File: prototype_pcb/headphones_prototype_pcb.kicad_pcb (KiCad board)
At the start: 2 copper layers, 59.8 x 62.2 mm, 52 parts, among them J1 LIGHTING_JACK, J2 CONN_01X10, J3 BOTTOM_FLEX_LIGHTNING, J4 CONN_01X10, J5 LIGHTNING_HEADPHONE_ADAPTER, J6 CONN_01X10, J7 IPHONE_HEADPHONE_JACK, J8 CONN_01X02, U1 SN74LVC1G123, U2 ADG774A, U3 SN74LVC1G123, U4 NC7S32

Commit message: Rigid prototype pcb v1.2
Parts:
- added J10: CONN_01X05, Pin_Headers:Pin_Header_Straight_1x05_Pitch2.54mm, F.Cu at (120.3, 128.8)
- added J9: LIGHTNING_HEADPHONE_ADAPTER, lightning_headphone_adapter:LIGHTNING_HEADPHONE_ADAPTER_HANDWIRE, F.Cu at (109.1, 83.3)
- J5: footprint lightning_headphone_adapter:LIGHTNING_HEADPHONE_ADAPTER -> lightning_headphone_adapter:LIGHTNING_HEADPHONE_ADAPTER_CASTELLATED
- moved J7 24.3 mm to (120.7, 142.4)
- moved J5 17.0 mm to (108.8, 107.8)
- moved G*** 5.35 mm to (134.2, 112.8)
- moved J1 3.37 mm to (112.5, 67.2)
- moved J3 0.13 mm to (162.1, 103.2)
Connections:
- J5 pad 11: Net-(J5-Pad11) -> Net-(J10-Pad2)
- J5 pad 12: Net-(J5-Pad12) -> Net-(J10-Pad5)
- J5 pad 13: Net-(J5-Pad13) -> Net-(J10-Pad4)
- J5 pad 14: Net-(J5-Pad14) -> Net-(J10-Pad1)
- J5 pad 16: Net-(J5-Pad12) -> Net-(J10-Pad5)
- J5 pad 17: Net-(J5-Pad14) -> Net-(J10-Pad1)
- J7 pad 1: Net-(J5-Pad12) -> Net-(J10-Pad1)
- J7 pad 2: Net-(J5-Pad13) -> Net-(J10-Pad2)
- J7 pad 4: Net-(J5-Pad11) -> Net-(J10-Pad4)
- J7 pad 5: Net-(J5-Pad14) -> Net-(J10-Pad5)
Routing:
- net Net-(J10-Pad5): track 0.00 -> 60.7 mm, vias 0 -> 2
- net Net-(J10-Pad1): track 0.00 -> 57.7 mm, vias 0 -> 3
- net Net-(J10-Pad4): track 0.00 -> 55.2 mm, vias 0 -> 2
- net Net-(J10-Pad2): track 0.00 -> 51.6 mm, vias 0 -> 1
- net Net-(J10-Pad3): track 4.51 -> 38.4 mm, vias 0 -> 2
- net Net-(J5-Pad9): track 26.8 -> 51.8 mm, vias 0 -> 2
- net Net-(J5-Pad7): track 25.8 -> 49.4 mm, vias 0 -> 2
- net Net-(J5-Pad8): track 27.1 -> 49.8 mm, vias 0 -> 2
- net Net-(J5-Pad6): track 24.6 -> 47.3 mm, vias 0 -> 2
- net /HPIN2: track 40.0 -> 62.3 mm, vias 2 -> 4
- net /HPIN4: track 42.7 -> 64.8 mm, vias 2 -> 4
- net /HPIN3: track 40.7 -> 62.5 mm, vias 2 -> 4
- net Net-(J5-Pad11): track 18.9 -> 0.00 mm
- net Net-(J5-Pad14): track 18.9 -> 0.00 mm, vias 2 -> 0
- net GNDREF: track 86.3 -> 104.3 mm, vias 4 -> 5
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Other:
- board size 59.8 x 62.2 mm -> 60.5 x 87 mm
- board text added: "iPhone 7 Headphone Jack Prototype v1.2"
- board text removed: "iPhone 7 Headphone Jack Prototype v1"

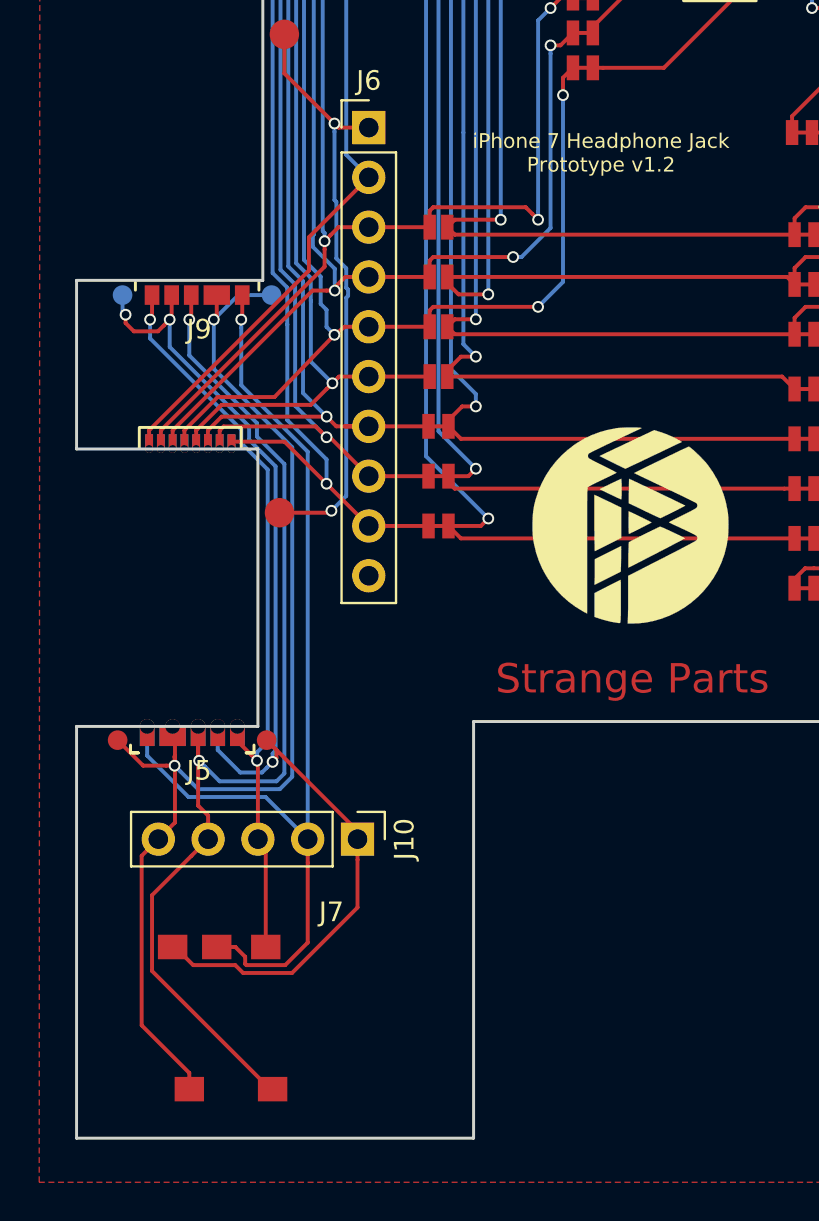
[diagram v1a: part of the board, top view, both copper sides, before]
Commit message: Remove castellated edges adapter from prototype
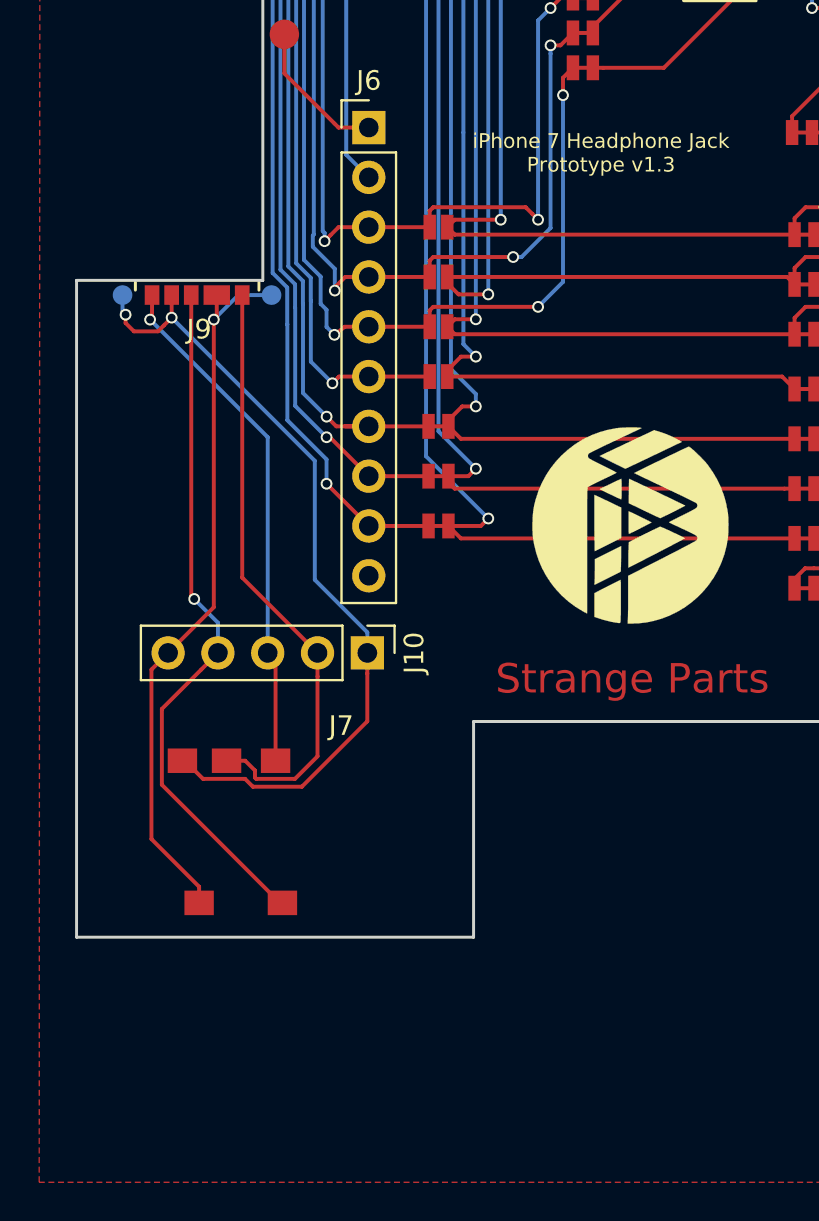
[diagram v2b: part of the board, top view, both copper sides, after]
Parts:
- removed J5: LIGHTNING_HEADPHONE_ADAPTER, lightning_headphone_adapter:LIGHTNING_HEADPHONE_ADAPTER_CASTELLATED
- moved J10 9.51 mm to (120.8, 119.2)
- moved J7 9.51 mm to (121.2, 132.9)
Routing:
- net Net-(J10-Pad5): track 60.7 -> 36.8 mm, vias 2 -> 1
- net Net-(J5-Pad1): track 30.5 -> 7.44 mm, vias 2 -> 0
- net Net-(J10-Pad2): track 51.6 -> 30.8 mm, vias 1 -> 0
- net Net-(J10-Pad4): track 55.2 -> 35.4 mm, vias 2 -> 1
- net GNDREF: track 104.3 -> 86.2 mm
- net Net-(J10-Pad1): track 57.7 -> 42.0 mm, vias 3 -> 2
- net /HPIN2: track 62.3 -> 48.7 mm
- net Net-(J10-Pad3): track 38.4 -> 26.4 mm, vias 2 -> 1
- net /HPIN3: track 62.5 -> 50.7 mm
- net /HPIN4: track 64.8 -> 54.5 mm
- net Net-(J5-Pad6): track 47.3 -> 38.8 mm
- net Net-(J5-Pad7): track 49.4 -> 42.5 mm
- net Net-(J5-Pad8): track 49.8 -> 43.5 mm
- net Net-(J5-Pad9): track 51.8 -> 46.0 mm
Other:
- board size 60.5 x 87 mm -> 60.5 x 76.8 mm
- board text added: "iPhone 7 Headphone Jack Prototype v1.3"
- board text removed: "iPhone 7 Headphone Jack Prototype v1.2"
